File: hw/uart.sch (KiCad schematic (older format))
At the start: 10 parts

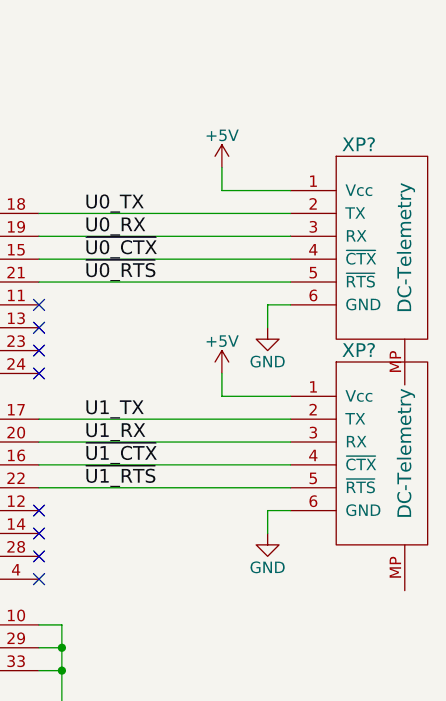
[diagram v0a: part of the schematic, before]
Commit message: hw: finish conn page
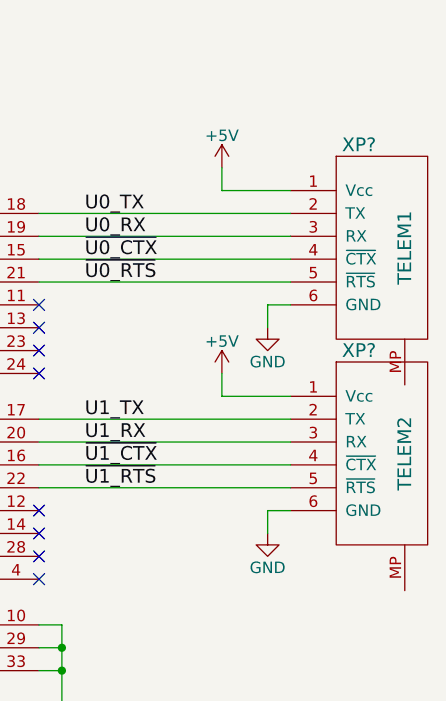
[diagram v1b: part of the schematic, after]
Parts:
- XP?: value DC-Telemetry -> TELEM1
- XP?: value DC-Telemetry -> TELEM2
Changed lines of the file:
@@
 P 6550 5750
 F 0 "XP?" H 6450 6200 60  0000 C CNN
-F 1 "DC-Telemetry" V 6650 5750 60  0000 C CNN
+F 1 "TELEM1" V 6650 5750 60  0000 C CNN
 F 2 "Connectors_JST:JST_GH_SM06B-GHS-TB_06x1.25mm_Angled" H 6550 5750 60  0001 C CNN
 F 3 "" H 6550 5750 60  0001 C CNN
@@
 P 6550 6650
 F 0 "XP?" H 6450 7100 60  0000 C CNN
-F 1 "DC-Telemetry" V 6650 6650 60  0000 C CNN
+F 1 "TELEM2" V 6650 6650 60  0000 C CNN
 F 2 "Connectors_JST:JST_GH_SM06B-GHS-TB_06x1.25mm_Angled" H 6550 6650 60  0001 C CNN
 F 3 "" H 6550 6650 60  0001 C CNN

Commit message: hw: sch ready
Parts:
- gave numbers to parts that had none: 10
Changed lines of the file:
@@
 $EndDescr
 $Comp
-L hat-ic:MAX3109 DD?
+L hat-ic:MAX3109 DD4
 U 1 1 5AB1B0A7
 P 4250 6600
-F 0 "DD?" H 3750 7800 60  0000 C CNN
+F 0 "DD4" H 3750 7800 60  0000 C CNN
 F 1 "MAX3109" H 4250 5400 60  0000 C CNN
 F 2 "Housings_DFN_QFN:QFN-32-1EP_5x5mm_Pitch0.5mm" H 4250 6300 60  0001 C CNN
@@
 Connection ~ 3350 8100
 $Comp
-L Device:R R?
+L Device:R R16
 U 1 1 5AB1B9A3
 P 3100 6250
-F 0 "R?" V 3180 6250 50  0000 C CNN
+F 0 "R16" V 3180 6250 50  0000 C CNN
 F 1 "10k" V 3100 6250 50  0000 C CNN
 F 2 "" V 3030 6250 50  0001 C CNN
@@
 Connection ~ 5150 7600
 $Comp
-L Device:R R?
+L Device:R R15
 U 1 1 5AB1D90A
 P 3150 5350
-F 0 "R?" V 3230 5350 50  0000 C CNN
+F 0 "R15" V 3230 5350 50  0000 C CNN
 F 1 "nc" V 3150 5350 50  0000 C CNN
 F 2 "" V 3080 5350 50  0001 C CNN
@@
 	3150 5200 3150 5100
 $Comp
-L dronecode-conn:DC-Telemetry XP?
+L dronecode-conn:DC-Telemetry XP6
 U 1 1 5AB2FA79
 P 6550 5750
-F 0 "XP?" H 6450 6200 60  0000 C CNN
+F 0 "XP6" H 6450 6200 60  0000 C CNN
 F 1 "TELEM1" V 6650 5750 60  0000 C CNN
 F 2 "Connectors_JST:JST_GH_SM06B-GHS-TB_06x1.25mm_Angled" H 6550 5750 60  0001 C CNN
@@
 $EndComp
 $Comp
-L dronecode-conn:DC-Telemetry XP?
+L dronecode-conn:DC-Telemetry XP7
 U 1 1 5AB2FFF0
 P 6550 6650
-F 0 "XP?" H 6450 7100 60  0000 C CNN
+F 0 "XP7" H 6450 7100 60  0000 C CNN
 F 1 "TELEM2" V 6650 6650 60  0000 C CNN
 F 2 "Connectors_JST:JST_GH_SM06B-GHS-TB_06x1.25mm_Angled" H 6550 6650 60  0001 C CNN
@@
 	6150 6800 5050 6800
 $Comp
-L power:+5V #PWR?
+L power:+5V #PWR041
 U 1 1 5AB3063A
 P 5850 5400
-F 0 "#PWR?" H 5850 5250 50  0001 C CNN
+F 0 "#PWR041" H 5850 5250 50  0001 C CNN
 F 1 "+5V" H 5850 5540 50  0000 C CNN
 F 2 "" H 5850 5400 50  0001 C CNN
@@
 	6050 6000 6050 6100
 $Comp
-L power:GND #PWR?
+L power:GND #PWR046
 U 1 1 5AB30BD8
 P 5150 7750
-F 0 "#PWR?" H 5150 7500 50  0001 C CNN
+F 0 "#PWR046" H 5150 7500 50  0001 C CNN
 F 1 "GND" H 5150 7600 50  0000 C CNN
 F 2 "" H 5150 7750 50  0001 C CNN
@@
 $EndComp
 $Comp
-L power:GND #PWR?
+L power:GND #PWR044
 U 1 1 5AB30BF8
 P 6050 7000
-F 0 "#PWR?" H 6050 6750 50  0001 C CNN
+F 0 "#PWR044" H 6050 6750 50  0001 C CNN
 F 1 "GND" H 6050 6850 50  0000 C CNN
 F 2 "" H 6050 7000 50  0001 C CNN
@@
 $EndComp
 $Comp
-L power:+5V #PWR?
+L power:+5V #PWR042
 U 1 1 5AB30E1E
 P 5850 6300
-F 0 "#PWR?" H 5850 6150 50  0001 C CNN
+F 0 "#PWR042" H 5850 6150 50  0001 C CNN
 F 1 "+5V" H 5850 6440 50  0000 C CNN
 F 2 "" H 5850 6300 50  0001 C CNN
@@
 ~U1_RTS
 $Comp
-L hat-ic:ASFL1 ZQ?
+L hat-ic:ASFL1 ZQ1
 U 1 1 5AB33753
 P 3900 3400
-F 0 "ZQ?" H 3750 3700 50  0000 C CNN
+F 0 "ZQ1" H 3750 3700 50  0000 C CNN
 F 1 "ASFL1-24.000MHZ-EC-T" H 3900 3000 50  0000 C CNN
 F 2 "Crystals:Crystal_SMD_Abracon_ABM3B-4pin_5.0x3.2mm" H 3900 3400 50  0001 C CNN
@@
 $EndComp
 $Comp
-L Device:C C?
+L Device:C C9
 U 1 1 5AB3478D
 P 3150 3900
-F 0 "C?" H 3175 4000 50  0000 L CNN
+F 0 "C9" H 3175 4000 50  0000 L CNN
 F 1 "0.1" H 3175 3800 50  0000 L CNN
 F 2 "" H 3188 3750 50  0001 C CNN
@@
 $EndComp
 $Comp
-L power:GND #PWR?
+L power:GND #PWR039
 U 1 1 5AB347BB
 P 3150 4250
-F 0 "#PWR?" H 3150 4000 50  0001 C CNN
+F 0 "#PWR039" H 3150 4000 50  0001 C CNN
 F 1 "GND" H 3150 4100 50  0000 C CNN
 F 2 "" H 3150 4250 50  0001 C CNN
@@
 	3150 5600 3450 5600
 $Comp
-L Jumper:Jumper_3_Open JP?
+L Jumper:Jumper_3_Open JP1
 U 1 1 5AB6CF92
 P 5200 2800
-F 0 "JP?" V 5246 2886 50  0000 L CNN
+F 0 "JP1" V 5246 2886 50  0000 L CNN
 F 1 "Jumper_3_Open" V 5155 2886 50  0000 L CNN
 F 2 "" H 5200 2800 50  0001 C CNN
@@
 	5200 3250 5200 3050
 $Comp
-L Device:C C?
+L Device:C C10
 U 1 1 5AC0F665
 P 3100 7850
-F 0 "C?" H 2700 8050 50  0000 L CNN
+F 0 "C10" H 2700 8050 50  0000 L CNN
 F 1 "0.1" H 2850 8050 50  0000 L CNN
 F 2 "" H 3138 7700 50  0001 C CNN
@@
 $EndComp
 $Comp
-L Device:C C?
+L Device:C C11
 U 1 1 5AC0F72E
 P 3350 7850
-F 0 "C?" H 2700 7950 50  0000 L CNN
+F 0 "C11" H 2700 7950 50  0000 L CNN
 F 1 "0.1" H 2850 7950 50  0000 L CNN
 F 2 "" H 3388 7700 50  0001 C CNN
@@
 $EndComp
 $Comp
-L power:+3.3V #PWR?
+L power:+3.3V #PWR038
 U 1 1 5AC2B996
 P 3150 3050
-F 0 "#PWR?" H 3150 2900 50  0001 C CNN
+F 0 "#PWR038" H 3150 2900 50  0001 C CNN
 F 1 "+3.3V" H 3165 3223 50  0000 C CNN
 F 2 "" H 3150 3050 50  0001 C CNN
@@
 $EndComp
 $Comp
-L power:+3.3V #PWR?
+L power:+3.3V #PWR040
 U 1 1 5AC2B9D6
 P 3150 5100
-F 0 "#PWR?" H 3150 4950 50  0001 C CNN
+F 0 "#PWR040" H 3150 4950 50  0001 C CNN
 F 1 "+3.3V" H 3165 5273 50  0000 C CNN
 F 2 "" H 3150 5100 50  0001 C CNN
@@
 $EndComp
 $Comp
-L power:+3.3V #PWR?
+L power:+3.3V #PWR043
 U 1 1 5AC2BA1D
 P 2750 6450
-F 0 "#PWR?" H 2750 6300 50  0001 C CNN
+F 0 "#PWR043" H 2750 6300 50  0001 C CNN
 F 1 "+3.3V" V 2765 6578 50  0000 L CNN
 F 2 "" H 2750 6450 50  0001 C CNN
@@
 $EndComp
 $Comp
-L power:+3.3V #PWR?
+L power:+3.3V #PWR045
 U 1 1 5AC2C6EA
 P 3100 7100
-F 0 "#PWR?" H 3100 6950 50  0001 C CNN
+F 0 "#PWR045" H 3100 6950 50  0001 C CNN
 F 1 "+3.3V" H 3115 7273 50  0000 C CNN
 F 2 "" H 3100 7100 50  0001 C CNN

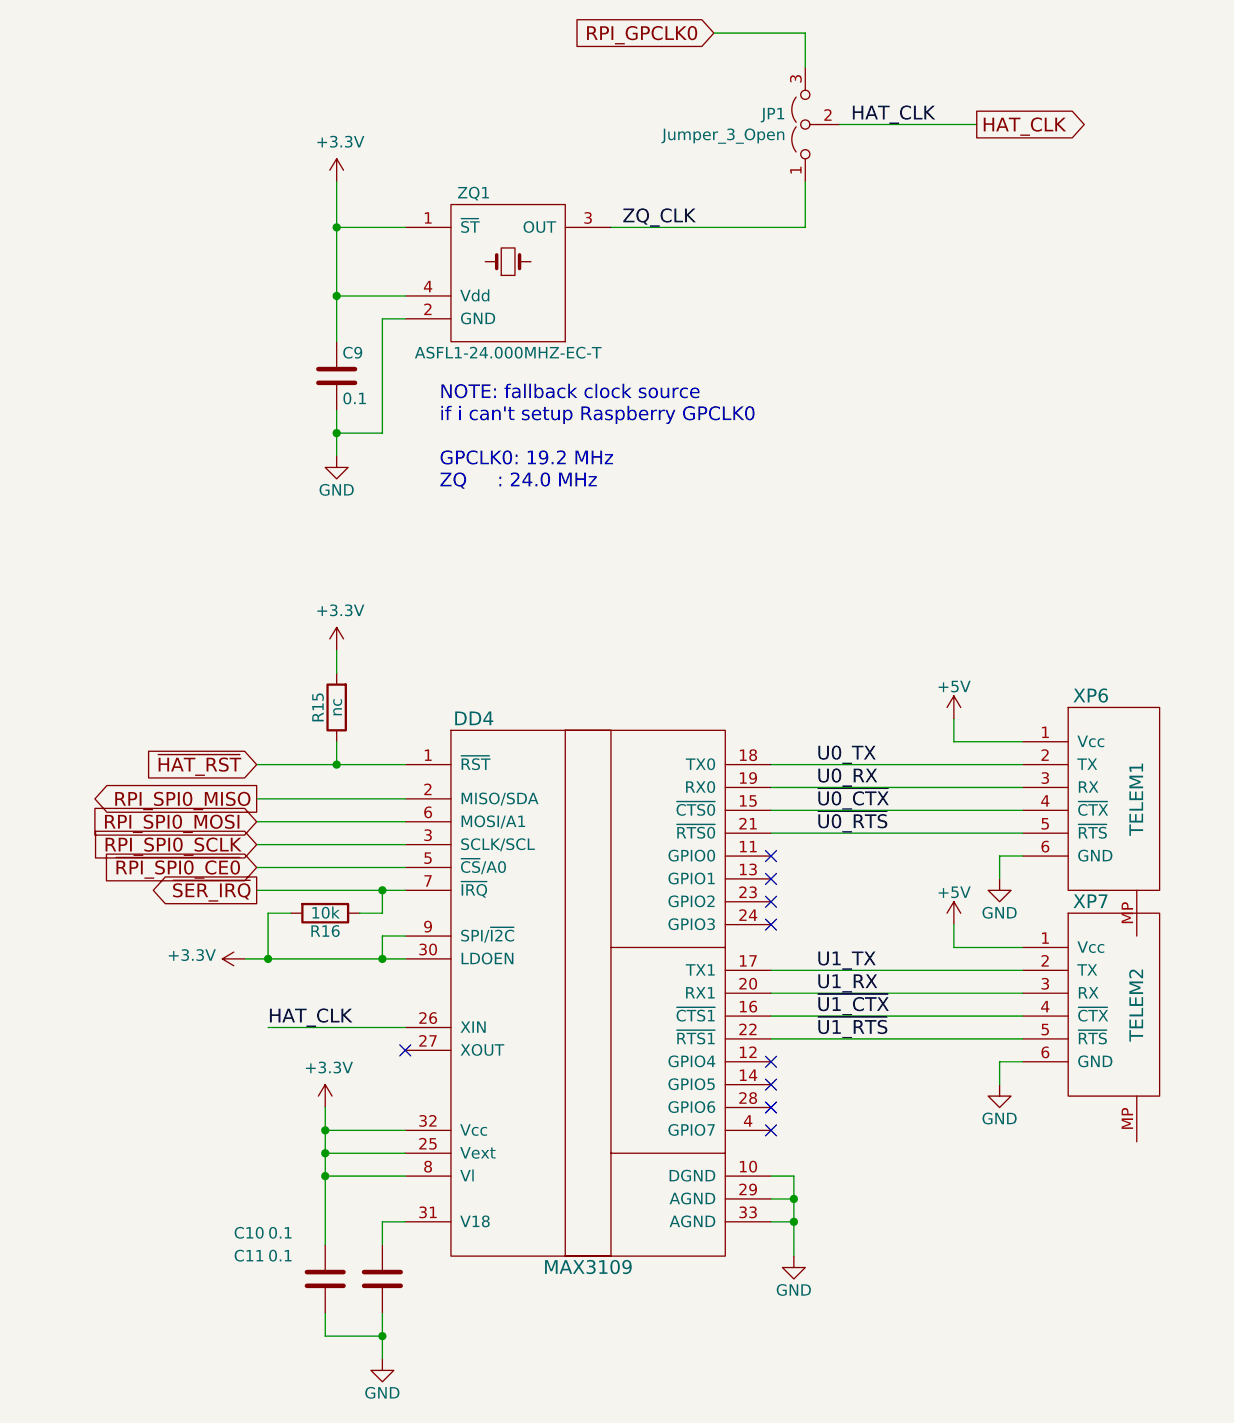
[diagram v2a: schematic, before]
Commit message: hw: cvpcb for R,C
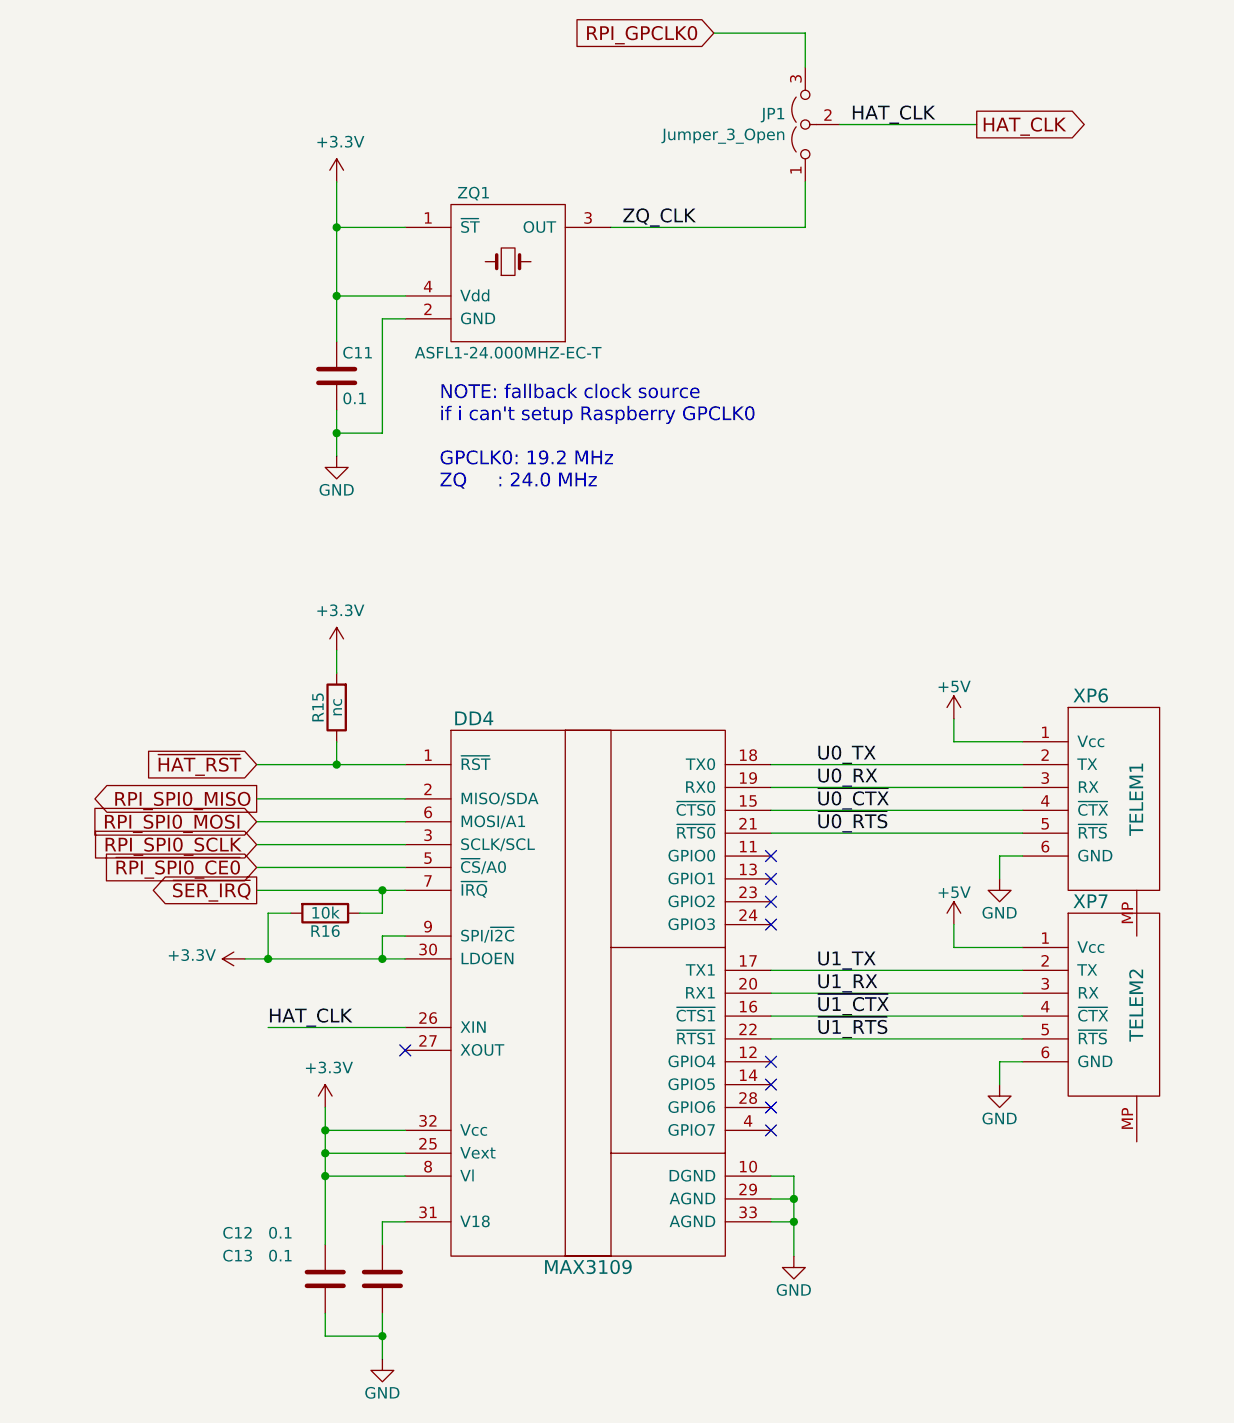
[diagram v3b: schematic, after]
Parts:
- C11: renamed from C9; footprint (none) -> Capacitor_SMD:C_0603_1608Metric
- C12: renamed from C10; footprint (none) -> Capacitor_SMD:C_0603_1608Metric
- C13: renamed from C11; footprint (none) -> Capacitor_SMD:C_0603_1608Metric
- R15, R16: footprint (none) -> Resistor_SMD:R_0603_1608Metric
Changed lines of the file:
@@
 $EndComp
 $Comp
-L power:GND #PWR014
+L power:GND #PWR046
 U 1 1 5AB1B2D7
 P 3350 8200
-F 0 "#PWR014" H 3350 7950 50  0001 C CNN
+F 0 "#PWR046" H 3350 7950 50  0001 C CNN
 F 1 "GND" H 3350 8050 50  0000 C CNN
 F 2 "" H 3350 8200 50  0001 C CNN
@@
 F 0 "R16" V 3180 6250 50  0000 C CNN
 F 1 "10k" V 3100 6250 50  0000 C CNN
-F 2 "" V 3030 6250 50  0001 C CNN
+F 2 "Resistor_SMD:R_0603_1608Metric" V 3030 6250 50  0001 C CNN
 F 3 "" H 3100 6250 50  0001 C CNN
 	1    3100 6250
@@
 Connection ~ 3350 6150
 $Comp
-L power:GND #PWR016
+L power:GND #PWR040
 U 1 1 5AB1C686
 P 6050 6100
-F 0 "#PWR016" H 6050 5850 50  0001 C CNN
+F 0 "#PWR040" H 6050 5850 50  0001 C CNN
 F 1 "GND" H 6050 5950 50  0000 C CNN
 F 2 "" H 6050 6100 50  0001 C CNN
@@
 F 0 "R15" V 3230 5350 50  0000 C CNN
 F 1 "nc" V 3150 5350 50  0000 C CNN
-F 2 "" V 3080 5350 50  0001 C CNN
+F 2 "Resistor_SMD:R_0603_1608Metric" V 3080 5350 50  0001 C CNN
 F 3 "" H 3150 5350 50  0001 C CNN
 	1    3150 5350
@@
 	6150 6800 5050 6800
 $Comp
-L power:+5V #PWR041
+L power:+5V #PWR039
 U 1 1 5AB3063A
 P 5850 5400
-F 0 "#PWR041" H 5850 5250 50  0001 C CNN
+F 0 "#PWR039" H 5850 5250 50  0001 C CNN
 F 1 "+5V" H 5850 5540 50  0000 C CNN
 F 2 "" H 5850 5400 50  0001 C CNN
@@
 	6050 6000 6050 6100
 $Comp
-L power:GND #PWR046
+L power:GND #PWR045
 U 1 1 5AB30BD8
 P 5150 7750
-F 0 "#PWR046" H 5150 7500 50  0001 C CNN
+F 0 "#PWR045" H 5150 7500 50  0001 C CNN
 F 1 "GND" H 5150 7600 50  0000 C CNN
 F 2 "" H 5150 7750 50  0001 C CNN
@@
 $EndComp
 $Comp
-L power:GND #PWR044
+L power:GND #PWR043
 U 1 1 5AB30BF8
 P 6050 7000
-F 0 "#PWR044" H 6050 6750 50  0001 C CNN
+F 0 "#PWR043" H 6050 6750 50  0001 C CNN
 F 1 "GND" H 6050 6850 50  0000 C CNN
 F 2 "" H 6050 7000 50  0001 C CNN
@@
 $EndComp
 $Comp
-L power:+5V #PWR042
+L power:+5V #PWR041
 U 1 1 5AB30E1E
 P 5850 6300
-F 0 "#PWR042" H 5850 6150 50  0001 C CNN
+F 0 "#PWR041" H 5850 6150 50  0001 C CNN
 F 1 "+5V" H 5850 6440 50  0000 C CNN
 F 2 "" H 5850 6300 50  0001 C CNN
@@
 $EndComp
 $Comp
-L Device:C C9
+L Device:C C11
 U 1 1 5AB3478D
 P 3150 3900
-F 0 "C9" H 3175 4000 50  0000 L CNN
+F 0 "C11" H 3175 4000 50  0000 L CNN
 F 1 "0.1" H 3175 3800 50  0000 L CNN
-F 2 "" H 3188 3750 50  0001 C CNN
+F 2 "Capacitor_SMD:C_0603_1608Metric" H 3188 3750 50  0001 C CNN
 F 3 "" H 3150 3900 50  0001 C CNN
 	1    3150 3900
@@
 $EndComp
 $Comp
-L power:GND #PWR039
+L power:GND #PWR037
 U 1 1 5AB347BB
 P 3150 4250
-F 0 "#PWR039" H 3150 4000 50  0001 C CNN
+F 0 "#PWR037" H 3150 4000 50  0001 C CNN
 F 1 "GND" H 3150 4100 50  0000 C CNN
 F 2 "" H 3150 4250 50  0001 C CNN
@@
 	5200 3250 5200 3050
 $Comp
-L Device:C C10
+L Device:C C12
 U 1 1 5AC0F665
 P 3100 7850
-F 0 "C10" H 2700 8050 50  0000 L CNN
+F 0 "C12" H 2650 8050 50  0000 L CNN
 F 1 "0.1" H 2850 8050 50  0000 L CNN
-F 2 "" H 3138 7700 50  0001 C CNN
+F 2 "Capacitor_SMD:C_0603_1608Metric" H 3138 7700 50  0001 C CNN
 F 3 "~" H 3100 7850 50  0001 C CNN
 	1    3100 7850
@@
 $EndComp
 $Comp
-L Device:C C11
+L Device:C C13
 U 1 1 5AC0F72E
 P 3350 7850
-F 0 "C11" H 2700 7950 50  0000 L CNN
+F 0 "C13" H 2650 7950 50  0000 L CNN
 F 1 "0.1" H 2850 7950 50  0000 L CNN
-F 2 "" H 3388 7700 50  0001 C CNN
+F 2 "Capacitor_SMD:C_0603_1608Metric" H 3388 7700 50  0001 C CNN
 F 3 "~" H 3350 7850 50  0001 C CNN
 	1    3350 7850
@@
 $EndComp
 $Comp
-L power:+3.3V #PWR038
+L power:+3.3V #PWR036
 U 1 1 5AC2B996
 P 3150 3050
-F 0 "#PWR038" H 3150 2900 50  0001 C CNN
+F 0 "#PWR036" H 3150 2900 50  0001 C CNN
 F 1 "+3.3V" H 3165 3223 50  0000 C CNN
 F 2 "" H 3150 3050 50  0001 C CNN
@@
 $EndComp
 $Comp
-L power:+3.3V #PWR040
+L power:+3.3V #PWR038
 U 1 1 5AC2B9D6
 P 3150 5100
-F 0 "#PWR040" H 3150 4950 50  0001 C CNN
+F 0 "#PWR038" H 3150 4950 50  0001 C CNN
 F 1 "+3.3V" H 3165 5273 50  0000 C CNN
 F 2 "" H 3150 5100 50  0001 C CNN
@@
 $EndComp
 $Comp
-L power:+3.3V #PWR043
+L power:+3.3V #PWR042
 U 1 1 5AC2BA1D
 P 2750 6450
-F 0 "#PWR043" H 2750 6300 50  0001 C CNN
+F 0 "#PWR042" H 2750 6300 50  0001 C CNN
 F 1 "+3.3V" V 2765 6578 50  0000 L CNN
 F 2 "" H 2750 6450 50  0001 C CNN
@@
 $EndComp
 $Comp
-L power:+3.3V #PWR045
+L power:+3.3V #PWR044
 U 1 1 5AC2C6EA
 P 3100 7100
-F 0 "#PWR045" H 3100 6950 50  0001 C CNN
+F 0 "#PWR044" H 3100 6950 50  0001 C CNN
 F 1 "+3.3V" H 3115 7273 50  0000 C CNN
 F 2 "" H 3100 7100 50  0001 C CNN

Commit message: hw: only custom packages left unassigned
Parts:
- JP1: footprint (none) -> Jumper:SolderJumper-3_P1.3mm_Open_RoundedPad1.0x1.5mm
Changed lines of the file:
@@
 F 0 "JP1" V 5246 2886 50  0000 L CNN
 F 1 "Jumper_3_Open" V 5155 2886 50  0000 L CNN
-F 2 "" H 5200 2800 50  0001 C CNN
+F 2 "Jumper:SolderJumper-3_P1.3mm_Open_RoundedPad1.0x1.5mm" H 5200 2800 50  0001 C CNN
 F 3 "~" H 5200 2800 50  0001 C CNN
 	1    5200 2800

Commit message: hw: wonring on NET
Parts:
- DD4: footprint Housings_DFN_QFN:QFN-32-1EP_5x5mm_Pitch0.5mm -> Package_DFN_QFN:QFN-32-1EP_5x5mm_P0.5mm_EP3.45x3.45mm
- XP6, XP7: footprint Connectors_JST:JST_GH_SM06B-GHS-TB_06x1.25mm_Angled -> Connector_JST:JST_GH_SM06B-GHS-TB_1x06-1MP_P1.25mm_Horizontal
- ZQ1: footprint Crystals:Crystal_SMD_Abracon_ABM3B-4pin_5.0x3.2mm -> Crystal:Crystal_SMD_Abracon_ABM3B-4Pin_5.0x3.2mm
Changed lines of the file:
@@
 F 0 "DD4" H 3750 7800 60  0000 C CNN
 F 1 "MAX3109" H 4250 5400 60  0000 C CNN
-F 2 "Housings_DFN_QFN:QFN-32-1EP_5x5mm_Pitch0.5mm" H 4250 6300 60  0001 C CNN
+F 2 "Package_DFN_QFN:QFN-32-1EP_5x5mm_P0.5mm_EP3.45x3.45mm" H 4250 6300 60  0001 C CNN
 F 3 "" H 4250 6300 60  0001 C CNN
 	1    4250 6600
@@
 F 0 "XP6" H 6450 6200 60  0000 C CNN
 F 1 "TELEM1" V 6650 5750 60  0000 C CNN
-F 2 "Connectors_JST:JST_GH_SM06B-GHS-TB_06x1.25mm_Angled" H 6550 5750 60  0001 C CNN
+F 2 "Connector_JST:JST_GH_SM06B-GHS-TB_1x06-1MP_P1.25mm_Horizontal" H 6550 5750 60  0001 C CNN
 F 3 "" H 6550 5750 60  0001 C CNN
 	1    6550 5750
@@
 F 0 "XP7" H 6450 7100 60  0000 C CNN
 F 1 "TELEM2" V 6650 6650 60  0000 C CNN
-F 2 "Connectors_JST:JST_GH_SM06B-GHS-TB_06x1.25mm_Angled" H 6550 6650 60  0001 C CNN
+F 2 "Connector_JST:JST_GH_SM06B-GHS-TB_1x06-1MP_P1.25mm_Horizontal" H 6550 6650 60  0001 C CNN
 F 3 "" H 6550 6650 60  0001 C CNN
 	1    6550 6650
@@
 F 0 "ZQ1" H 3750 3700 50  0000 C CNN
 F 1 "ASFL1-24.000MHZ-EC-T" H 3900 3000 50  0000 C CNN
-F 2 "Crystals:Crystal_SMD_Abracon_ABM3B-4pin_5.0x3.2mm" H 3900 3400 50  0001 C CNN
+F 2 "Crystal:Crystal_SMD_Abracon_ABM3B-4Pin_5.0x3.2mm" H 3900 3400 50  0001 C CNN
 F 3 "https://www.terraelectronica.ru/pdf/show?pdf_file=%252Fds%252Fpdf%252FA%252FASFL1-24.pdf" H 3900 3400 50  0001 C CNN
 	1    3900 3400

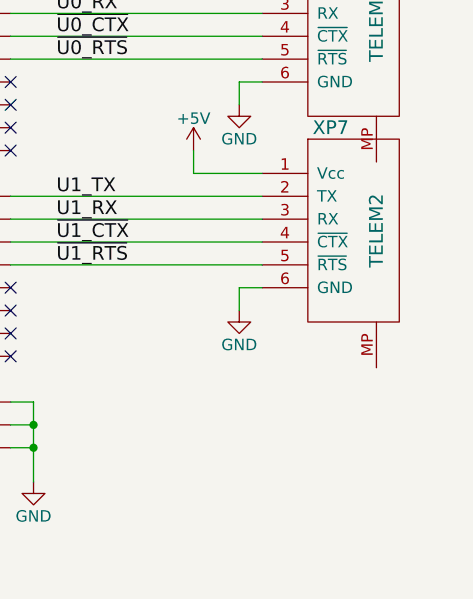
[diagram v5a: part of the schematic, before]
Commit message: hw: connect GH mount points with GND, add 3V battery
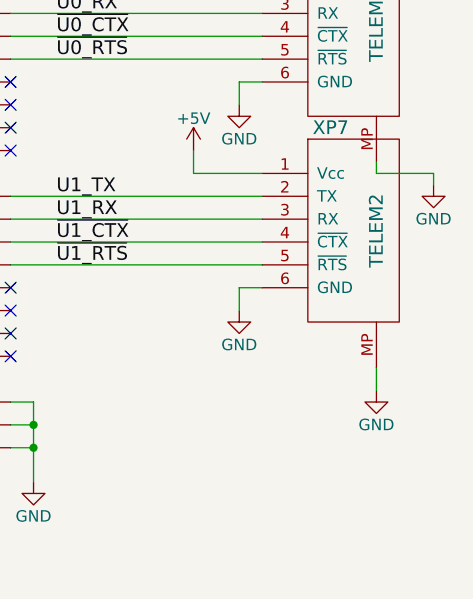
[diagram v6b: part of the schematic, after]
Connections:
- net GND: now also XP6.MP, XP7.MP
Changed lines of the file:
@@
 	1    0    0    -1
 $EndComp
+$Comp
+L power:GND #PWR?
+U 1 1 5ACF9FBD
+P 6650 7350
+F 0 "#PWR?" H 6650 7100 50  0001 C CNN
+F 1 "GND" H 6650 7200 50  0000 C CNN
+F 2 "" H 6650 7350 50  0001 C CNN
+F 3 "" H 6650 7350 50  0001 C CNN
+	1    6650 7350
+	1    0    0    -1
+$EndComp
+$Comp
+L power:GND #PWR?
+U 1 1 5ACFA00F
+P 6900 6450
+F 0 "#PWR?" H 6900 6200 50  0001 C CNN
+F 1 "GND" H 6900 6300 50  0000 C CNN
+F 2 "" H 6900 6450 50  0001 C CNN
+F 3 "" H 6900 6450 50  0001 C CNN
+	1    6900 6450
+	1    0    0    -1
+$EndComp
+Wire Wire Line
+	6900 6450 6900 6400
+Wire Wire Line
+	6900 6400 6650 6400
+Wire Wire Line
+	6650 6400 6650 6350
+Wire Wire Line
+	6650 7350 6650 7250
 $EndSCHEMATC
